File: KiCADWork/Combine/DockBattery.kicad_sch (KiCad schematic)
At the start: 28 parts, among them U2 TPS61023DRLR, U3 AMS1117-3.3, U4 BQ24073RGT

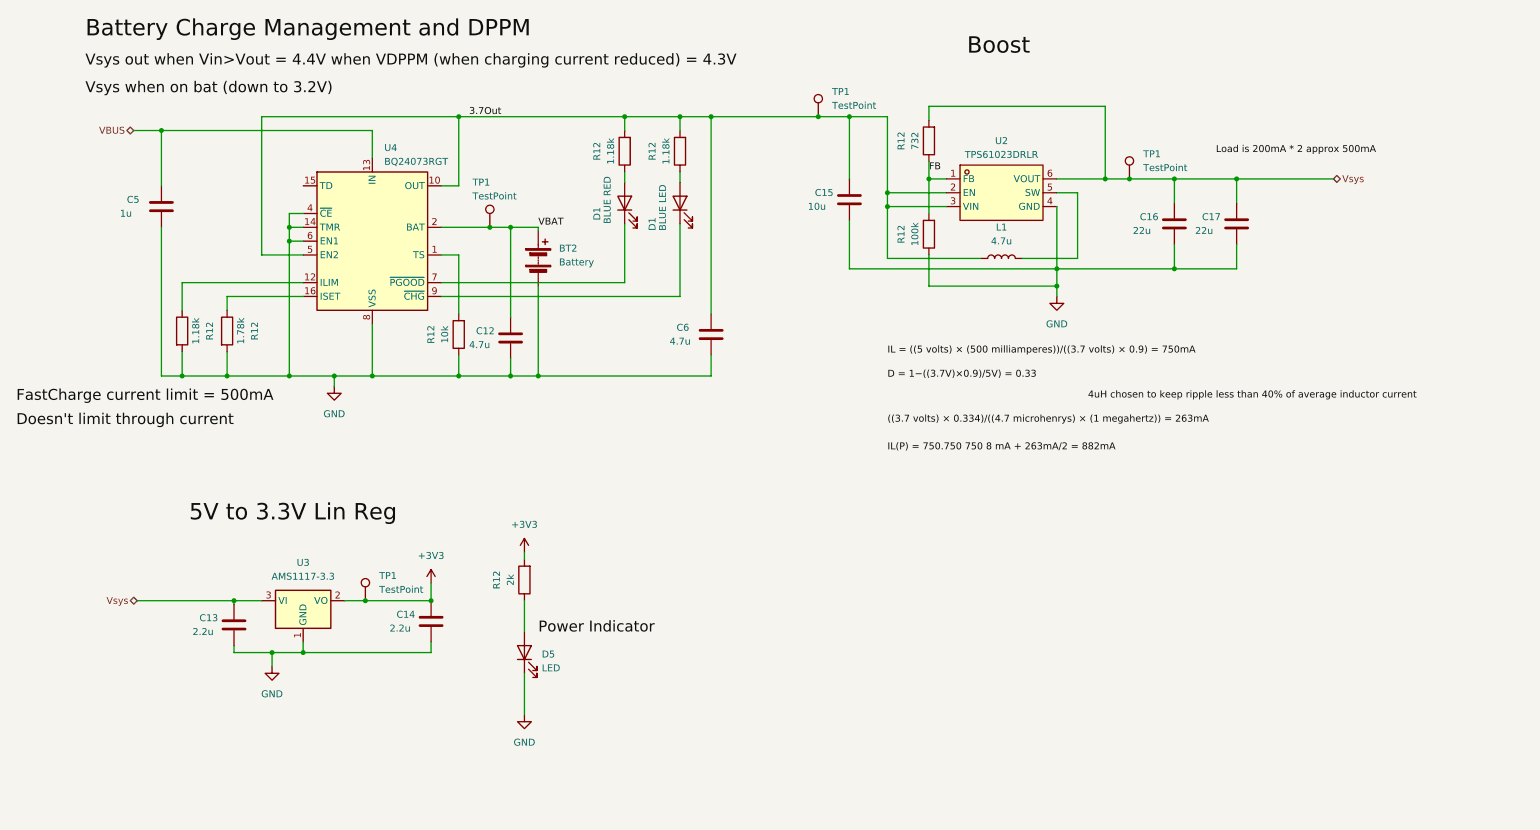
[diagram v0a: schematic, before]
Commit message: Completing the combined layout
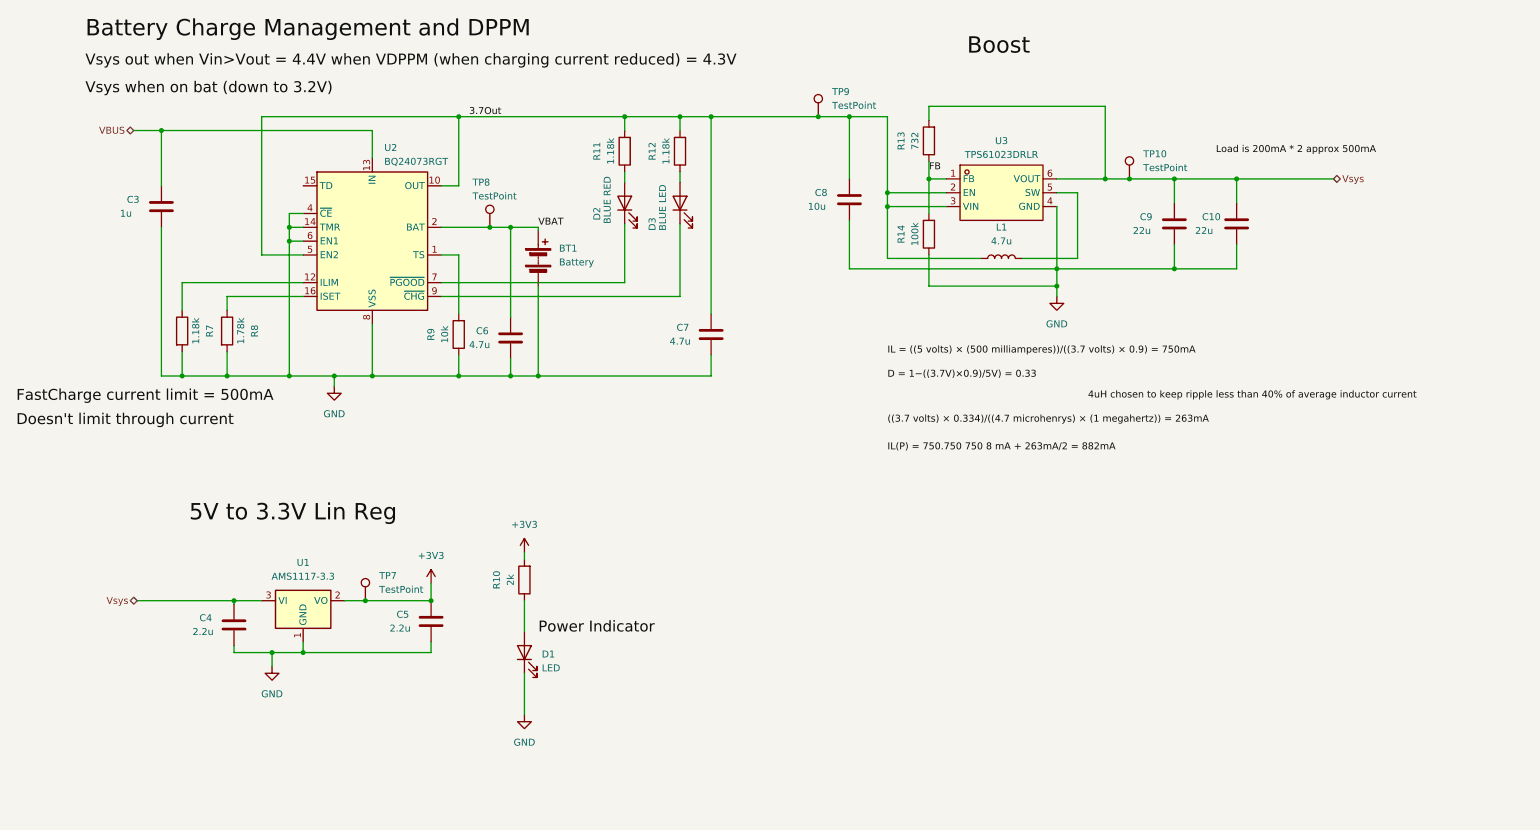
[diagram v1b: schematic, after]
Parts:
- renumbered BT2 to BT1, C17 to C10, C5 to C3, C13 to C4, C14 to C5, C12 to C6, C6 to C7, C15 to C8, C16 to C9, D5 to D1, D1 to D2, D1 to D3, R12 to R10, R12 to R11, R12 to R13, R12 to R14, R12 to R7, R12 to R8, R12 to R9, TP1 to TP10, TP1 to TP7, TP1 to TP8, TP1 to TP9, U3 to U1, U4 to U2, U2 to U3

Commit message: Schem rev 1 pt1
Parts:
- added C62: 10u, Capacitor_SMD:C_0402_1005Metric_Pad0.74x0.62mm_HandSolder, symbol Device:C
- L1: footprint easyeda2kicad:IND-SMD_L5.2-W5.2_YSPI0530 -> easyeda2kicad:IND-SMD_L4.4-W4.2
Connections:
- net GND: now also U2.15 (TD), C62.2
- net VBUS: now also C62.1
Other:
- moved on the sheet: C4, C5, D1, R10, TP7, U1
